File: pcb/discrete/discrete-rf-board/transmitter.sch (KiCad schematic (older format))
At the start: 8 parts

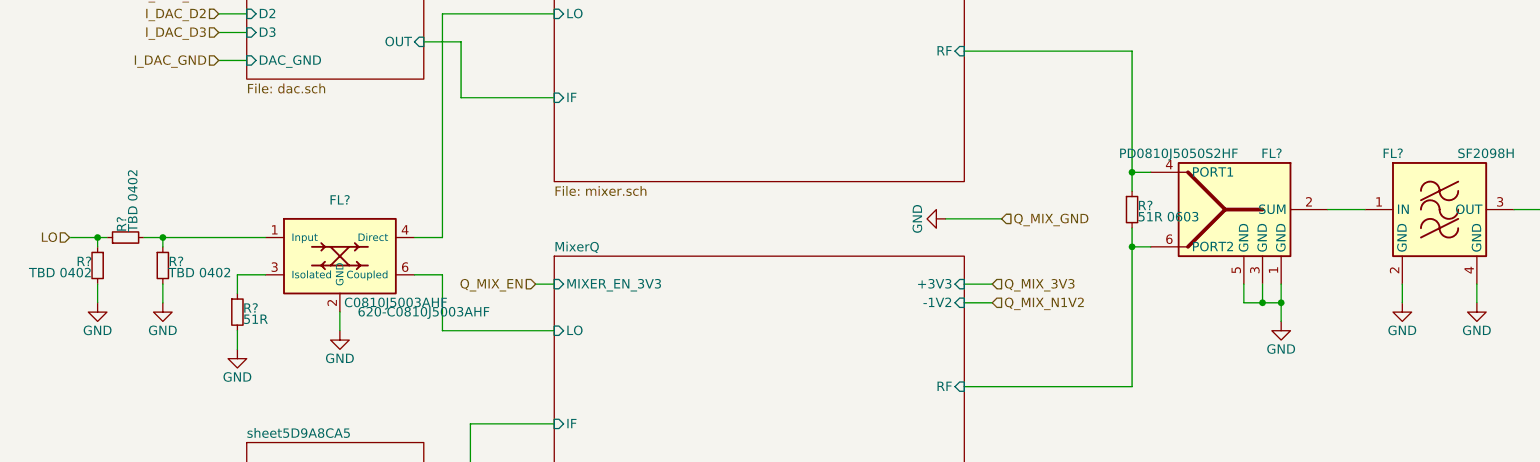
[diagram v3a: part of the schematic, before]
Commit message: Add matching PNP/NPN transistor pairs, fix pin numbering for BFU520R transistors TODO fix biasing on power stage, source last NPN transistor, autofill and start sourcing passives
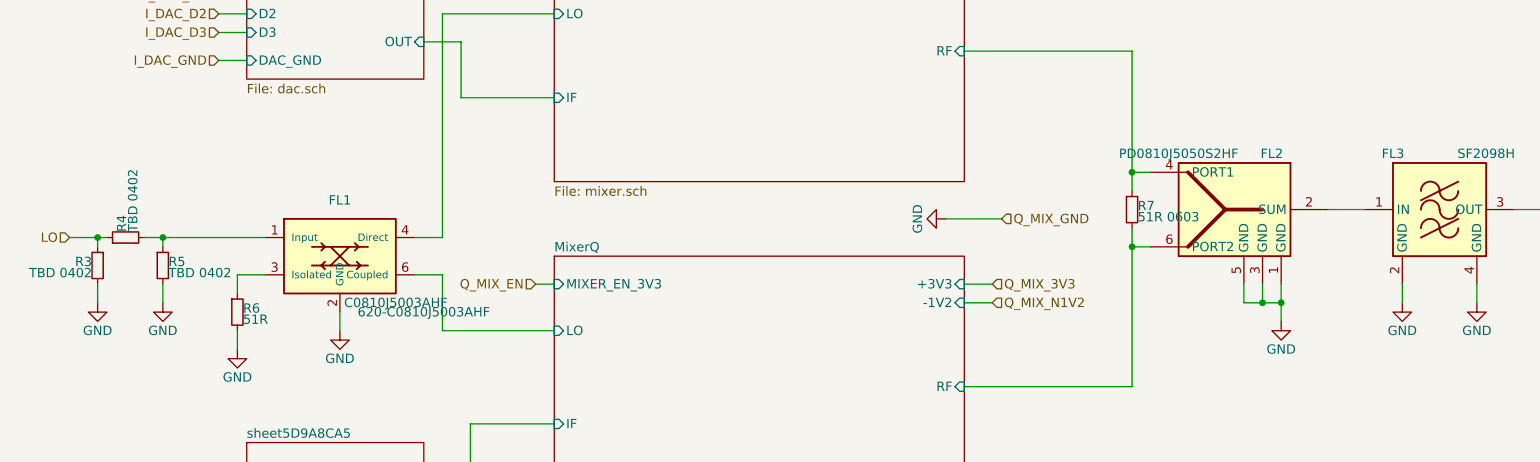
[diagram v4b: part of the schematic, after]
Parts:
- gave numbers to parts that had none: 8
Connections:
- net at FL2.2 (SUM): now also FL3.1 (IN)
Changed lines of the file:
@@
 NOTE: power supplies should be separated so that\nwe don't need to route on this board
 $Comp
-L discrete-parts:PD0810J5050S2HF FL?
+L discrete-parts:PD0810J5050S2HF FL2
 U 1 1 5D7F3EFF
 P 7250 3550
-F 0 "FL?" H 7000 3850 50  0000 C CNN
+F 0 "FL2" H 7000 3850 50  0000 C CNN
 F 1 "PD0810J5050S2HF" H 7500 3850 50  0000 C CNN
 F 2 "" H 7150 3100 50  0001 C CNN
@@
 	6750 3750 6850 3750
 $Comp
-L Device:R_Small R?
+L Device:R_Small R7
 U 1 1 5D7F54C0
 P 6750 3550
-F 0 "R?" H 6780 3570 50  0000 L CNN
+F 0 "R7" H 6780 3570 50  0000 L CNN
 F 1 "51R 0603" H 6780 3510 50  0000 L CNN
 F 2 "" H 6750 3550 50  0001 C CNN
@@
 Connection ~ 6750 3350
 $Comp
-L power:GND #PWR?
+L power:GND #PWR026
 U 1 1 5D7F5C8F
 P 7550 4150
-F 0 "#PWR?" H 7550 3900 50  0001 C CNN
+F 0 "#PWR026" H 7550 3900 50  0001 C CNN
 F 1 "GND" H 7550 4000 50  0000 C CNN
 F 2 "" H 7550 4150 50  0001 C CNN
@@
 $EndSheet
 $Comp
-L discrete-parts:C0810J5003AHF FL?
+L discrete-parts:C0810J5003AHF FL1
 U 1 1 5D8BF3D9
 P 2500 3500
-F 0 "FL?" H 2500 3500 50  0000 C CNN
+F 0 "FL1" H 2500 3500 50  0000 C CNN
 F 1 "C0810J5003AHF" H 2800 2950 50  0000 C CNN
 F 2 "" H 2500 3500 50  0001 C CNN
@@
 $EndComp
 $Comp
-L Device:R_Small R?
+L Device:R_Small R4
 U 1 1 5D8C4C7E
 P 1350 3700
-F 0 "R?" H 1380 3720 50  0000 L CNN
+F 0 "R4" H 1380 3720 50  0000 L CNN
 F 1 "TBD 0402" H 1380 3660 50  0000 L CNN
 F 2 "" H 1350 3700 50  0001 C CNN
@@
 $EndComp
 $Comp
-L Device:R_Small R?
+L Device:R_Small R3
 U 1 1 5D8C5237
 P 1200 3850
-F 0 "R?" H 1230 3870 50  0000 L CNN
+F 0 "R3" H 1230 3870 50  0000 L CNN
 F 1 "TBD 0402" H 1230 3810 50  0000 L CNN
 F 2 "" H 1200 3850 50  0001 C CNN
@@
 $EndComp
 $Comp
-L Device:R_Small R?
+L Device:R_Small R5
 U 1 1 5D8C562D
 P 1550 3850
-F 0 "R?" H 1580 3870 50  0000 L CNN
+F 0 "R5" H 1580 3870 50  0000 L CNN
 F 1 "TBD 0402" H 1580 3810 50  0000 L CNN
 F 2 "" H 1550 3850 50  0001 C CNN
@@
 	2900 3900 3050 3900
 $Comp
-L Device:R_Small R?
+L Device:R_Small R6
 U 1 1 5D8C70E2
 P 1950 4100
-F 0 "R?" H 1980 4120 50  0000 L CNN
+F 0 "R6" H 1980 4120 50  0000 L CNN
 F 1 "51R" H 1980 4060 50  0000 L CNN
 F 2 "" H 1950 4100 50  0001 C CNN
@@
 	1200 3700 1250 3700
 $Comp
-L power:GND #PWR?
+L power:GND #PWR020
 U 1 1 5D8C821A
 P 1200 4050
-F 0 "#PWR?" H 1200 3800 50  0001 C CNN
+F 0 "#PWR020" H 1200 3800 50  0001 C CNN
 F 1 "GND" H 1200 3900 50  0000 C CNN
 F 2 "" H 1200 4050 50  0001 C CNN
@@
 	1200 4050 1200 3950
 $Comp
-L power:GND #PWR?
+L power:GND #PWR021
 U 1 1 5D8C8A04
 P 1550 4050
-F 0 "#PWR?" H 1550 3800 50  0001 C CNN
+F 0 "#PWR021" H 1550 3800 50  0001 C CNN
 F 1 "GND" H 1550 3900 50  0000 C CNN
 F 2 "" H 1550 4050 50  0001 C CNN
@@
 	1550 4050 1550 3950
 $Comp
-L power:GND #PWR?
+L power:GND #PWR022
 U 1 1 5D8C95C0
 P 1950 4300
-F 0 "#PWR?" H 1950 4050 50  0001 C CNN
+F 0 "#PWR022" H 1950 4050 50  0001 C CNN
 F 1 "GND" H 1950 4150 50  0000 C CNN
 F 2 "" H 1950 4300 50  0001 C CNN
@@
 	1950 4300 1950 4200
 $Comp
-L power:GND #PWR?
+L power:GND #PWR023
 U 1 1 5D8CA782
 P 2500 4200
-F 0 "#PWR?" H 2500 3950 50  0001 C CNN
+F 0 "#PWR023" H 2500 3950 50  0001 C CNN
 F 1 "GND" H 2500 4050 50  0000 C CNN
 F 2 "" H 2500 4200 50  0001 C CNN
@@
 P 8400 3550
 AR Path="/5CA6B0AA/5DCA527D" Ref="FL?"  Part="1"
-AR Path="/5CA6B0B3/5DCA527D" Ref="FL?"  Part="1"
-F 0 "FL?" H 8150 3850 50  0000 C CNN
+AR Path="/5CA6B0B3/5DCA527D" Ref="FL3"  Part="1"
+F 0 "FL3" H 8150 3850 50  0000 C CNN
 F 1 "SF2098H" H 8650 3850 50  0000 C CNN
 F 2 "" H 8400 3100 50  0001 C CNN
@@
 	7800 3550 8000 3550
 $Comp
-L power:GND #PWR?
+L power:GND #PWR027
 U 1 1 5DCABC6C
 P 8200 4050
-F 0 "#PWR?" H 8200 3800 50  0001 C CNN
+F 0 "#PWR027" H 8200 3800 50  0001 C CNN
 F 1 "GND" H 8200 3900 50  0000 C CNN
 F 2 "" H 8200 4050 50  0001 C CNN
@@
 $EndComp
 $Comp
-L power:GND #PWR?
+L power:GND #PWR028
 U 1 1 5DCABEC4
 P 8600 4050
-F 0 "#PWR?" H 8600 3800 50  0001 C CNN
+F 0 "#PWR028" H 8600 3800 50  0001 C CNN
 F 1 "GND" H 8600 3900 50  0000 C CNN
 F 2 "" H 8600 4050 50  0001 C CNN
@@
 PA_GND
 $Comp
-L power:GND #PWR?
+L power:GND #PWR029
 U 1 1 5D8EC555
 P 10400 2700
-F 0 "#PWR?" H 10400 2450 50  0001 C CNN
+F 0 "#PWR029" H 10400 2450 50  0001 C CNN
 F 1 "GND" H 10400 2550 50  0000 C CNN
 F 2 "" H 10400 2700 50  0001 C CNN
@@
 I_MIX_GND
 $Comp
-L power:GND #PWR?
+L power:GND #PWR025
 U 1 1 5D8EF6D5
 P 5800 1900
-F 0 "#PWR?" H 5800 1650 50  0001 C CNN
+F 0 "#PWR025" H 5800 1650 50  0001 C CNN
 F 1 "GND" H 5800 1750 50  0000 C CNN
 F 2 "" H 5800 1900 50  0001 C CNN
@@
 Q_MIX_GND
 $Comp
-L power:GND #PWR?
+L power:GND #PWR024
 U 1 1 5D8F1675
 P 5750 3600
-F 0 "#PWR?" H 5750 3350 50  0001 C CNN
+F 0 "#PWR024" H 5750 3350 50  0001 C CNN
 F 1 "GND" H 5750 3450 50  0000 C CNN
 F 2 "" H 5750 3600 50  0001 C CNN

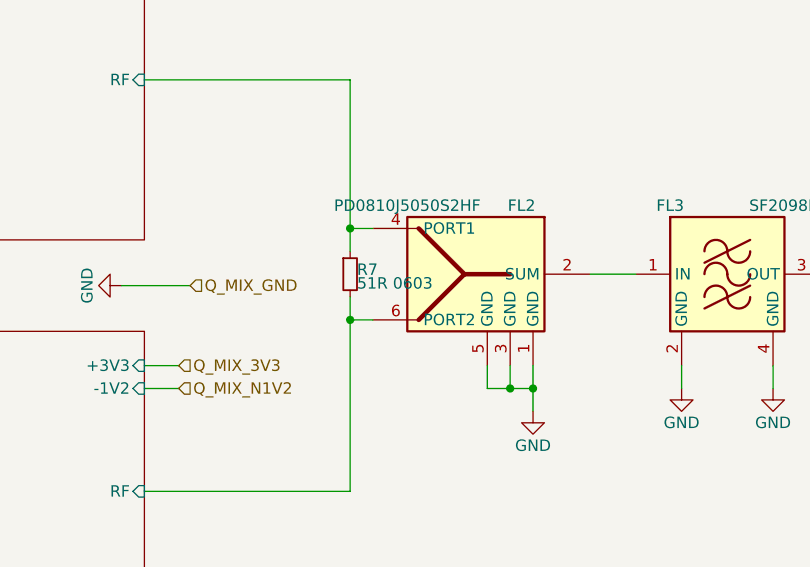
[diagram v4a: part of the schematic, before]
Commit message: All component values set (TODO change transistor gain stages to match values from experimentation
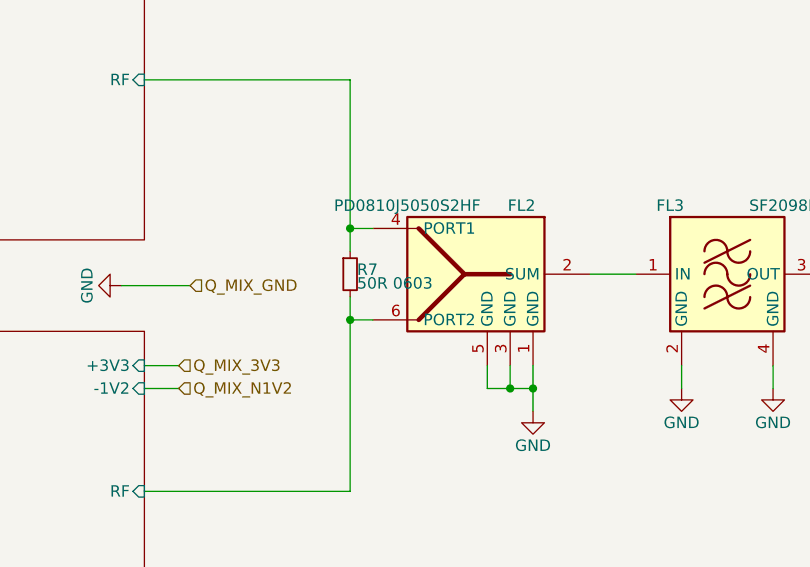
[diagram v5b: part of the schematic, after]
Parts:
- R7: value 51R 0603 -> 50R 0603
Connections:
- net at FL2.2 (SUM): now also FL3.1 (IN)
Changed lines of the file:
@@
 P 6750 3550
 F 0 "R7" H 6780 3570 50  0000 L CNN
-F 1 "51R 0603" H 6780 3510 50  0000 L CNN
+F 1 "50R 0603" H 6780 3510 50  0000 L CNN
 F 2 "" H 6750 3550 50  0001 C CNN
 F 3 "~" H 6750 3550 50  0001 C CNN

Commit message: Autofill; lots left to do
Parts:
- FL1: footprint (none) -> discrete_footprints:Anaren_C0810J5003AHF
- FL2: footprint (none) -> discrete_footprints:Anaren_PD0810J5050S2HF; Mouser (none) -> 620-PD0810J5050S2HF
- FL3: footprint (none) -> discrete_footprints:Murata_SM2016-4; Mouser (none) -> 719-SF2098H
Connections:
- net at FL2.2 (SUM): now also FL3.1 (IN)
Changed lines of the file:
@@
 F 0 "FL2" H 7000 3850 50  0000 C CNN
 F 1 "PD0810J5050S2HF" H 7500 3850 50  0000 C CNN
-F 2 "" H 7150 3100 50  0001 C CNN
+F 2 "discrete_footprints:Anaren_PD0810J5050S2HF" H 7150 3100 50  0001 C CNN
 F 3 "" H 7550 3000 50  0001 C CNN
+F 4 " 620-PD0810J5050S2HF" H 7550 3000 50  0001 C CNN "Mouser"
 	1    7250 3550
 	-1   0    0    -1
@@
 F 0 "FL1" H 2500 3500 50  0000 C CNN
 F 1 "C0810J5003AHF" H 2800 2950 50  0000 C CNN
-F 2 "" H 2500 3500 50  0001 C CNN
+F 2 "discrete_footprints:Anaren_C0810J5003AHF" H 2500 3500 50  0001 C CNN
 F 3 "" H 2500 3500 50  0001 C CNN
 F 4 " 620-C0810J5003AHF " H 2950 2900 50  0000 C CNN "Mouser"
@@
 F 0 "FL3" H 8150 3850 50  0000 C CNN
 F 1 "SF2098H" H 8650 3850 50  0000 C CNN
-F 2 "" H 8400 3100 50  0001 C CNN
+F 2 "discrete_footprints:Murata_SM2016-4" H 8400 3100 50  0001 C CNN
 F 3 "" H 8400 3950 50  0001 C CNN
+F 4 "719-SF2098H " H 8400 3950 50  0001 C CNN "Mouser"
 	1    8400 3550
 	1    0    0    -1

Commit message: Footprint some stuff
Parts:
- R4: footprint (none) -> Resistor_SMD:R_0402_1005Metric; Mouser (none) -> NoPart
- R6: value 51R -> 50R
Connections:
- net at FL2.2 (SUM): now also FL3.1 (IN)
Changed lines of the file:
@@
 F 0 "R4" H 1380 3720 50  0000 L CNN
 F 1 "TBD 0402" H 1380 3660 50  0000 L CNN
-F 2 "" H 1350 3700 50  0001 C CNN
+F 2 "Resistor_SMD:R_0402_1005Metric" H 1350 3700 50  0001 C CNN
 F 3 "~" H 1350 3700 50  0001 C CNN
+F 4 "NoPart" H 1350 3700 50  0001 C CNN "Mouser"
 	1    1350 3700
 	0    -1   -1   0
@@
 P 1950 4100
 F 0 "R6" H 1980 4120 50  0000 L CNN
-F 1 "51R" H 1980 4060 50  0000 L CNN
+F 1 "50R" H 1980 4060 50  0000 L CNN
 F 2 "" H 1950 4100 50  0001 C CNN
 F 3 "~" H 1950 4100 50  0001 C CNN

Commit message: Autofill
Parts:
- R3, R5: footprint (none) -> Resistor_SMD:R_0402_1005Metric; Mouser (none) -> NoPart
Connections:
- net at FL2.2 (SUM): now also FL3.1 (IN)
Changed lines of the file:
@@
 F 0 "R3" H 1230 3870 50  0000 L CNN
 F 1 "TBD 0402" H 1230 3810 50  0000 L CNN
-F 2 "" H 1200 3850 50  0001 C CNN
+F 2 "Resistor_SMD:R_0402_1005Metric" H 1200 3850 50  0001 C CNN
 F 3 "~" H 1200 3850 50  0001 C CNN
+F 4 "NoPart" H 1200 3850 50  0001 C CNN "Mouser"
 	1    1200 3850
 	-1   0    0    -1
@@
 F 0 "R5" H 1580 3870 50  0000 L CNN
 F 1 "TBD 0402" H 1580 3810 50  0000 L CNN
-F 2 "" H 1550 3850 50  0001 C CNN
+F 2 "Resistor_SMD:R_0402_1005Metric" H 1550 3850 50  0001 C CNN
 F 3 "~" H 1550 3850 50  0001 C CNN
+F 4 "NoPart" H 1550 3850 50  0001 C CNN "Mouser"
 	1    1550 3850
 	1    0    0    -1
